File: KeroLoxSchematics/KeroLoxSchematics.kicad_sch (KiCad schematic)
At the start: 49 parts, among them J1 Ignitor1_Output, J2 Ignitor2_Output, M1 LOX_Injector, M2 LOX_Dump, M3 LOX_Vent_Valve, M4 Kero_Vent_Valve, U10 Kero_Tank_PT, U11 LOX_Inj_Line_PT, U12 Kero_Inj_Line_PT, U13 Combusion_Chamber_PT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

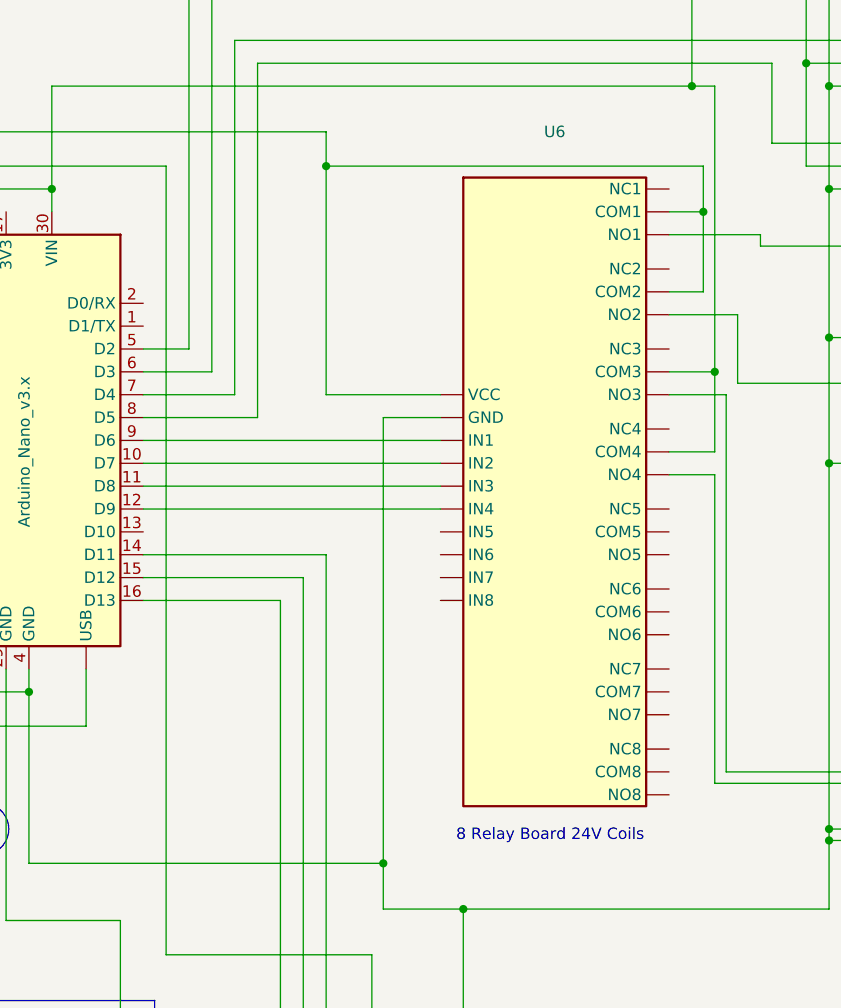
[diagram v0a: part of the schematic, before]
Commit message: Small Change in Relay Board Wiring
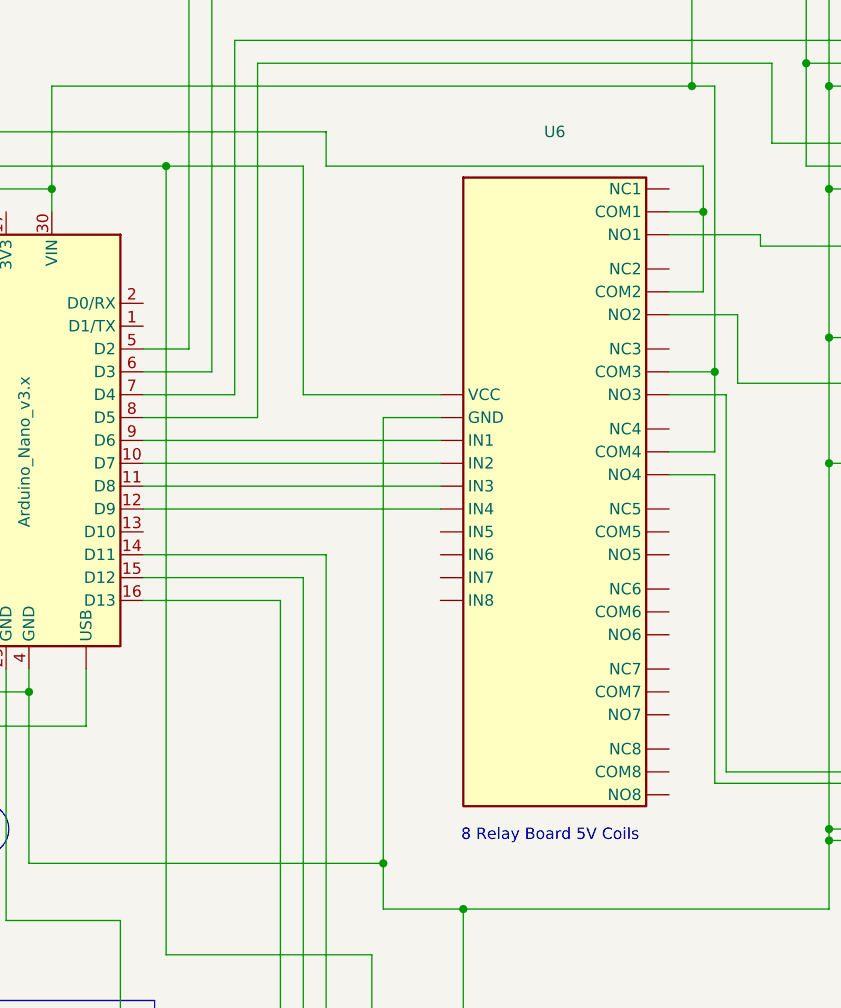
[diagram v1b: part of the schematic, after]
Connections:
- net at U15.9 (SHIELD): no longer U17.9 (SHIELD)
- net at U14.9 (SHIELD): now also U16.9 (SHIELD)
- net at A1.27 (+5V), U18.3 (CS), U18.6 (5V): now also U6. (NO8)
- new net: U15.9 (SHIELD), U17.9 (SHIELD)
- new net: U19. (Ethernet4), U20. (POE_OUT)
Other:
- note added: "8 Relay Board 5V Coils"
- note removed: "8 Relay Board 24V Coils"
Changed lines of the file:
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@@
 		)
 	)
-	(text "8 Relay Board 24V Coils"
+	(text "8 Relay Board 5V Coils"
 		(exclude_from_sim no)
 		(at 441.452 211.582 0)
@@
 	)
 	(junction
-		(at 416.56 137.16)
-		(diameter 0)
-		(color 255 153 0 1)
-	)
-	(junction
 		(at 393.7 238.76)
 		(diameter 0)
@@
 	)
 	(junction
+		(at 398.78 137.16)
+		(diameter 0)
+		(color 72 72 0 1)
+	)
+	(junction
 		(at 316.23 162.56)
 		(diameter 0)
@@
 	(wire
 		(pts
+			(xy 414.02 137.16) (xy 414.02 162.56)
+		)
+		(stroke
+			(width 0)
+			(type default)
+			(color 128 77 0 1)
+		)
+	)
+	(wire
+		(pts
 			(xy 147.32 207.01) (xy 173.99 207.01)
 		)
@@
 	(wire
 		(pts
-			(xy 416.56 137.16) (xy 416.56 162.56)
-		)
-		(stroke
-			(width 0)
-			(type default)
-			(color 255 153 0 1)
-		)
-	)
-	(wire
-		(pts
 			(xy 349.25 140.97) (xy 346.71 140.97)
 		)
@@
 	(wire
 		(pts
-			(xy 416.56 162.56) (xy 429.26 162.56)
-		)
-		(stroke
-			(width 0)
-			(type default)
-			(color 255 153 0 1)
-		)
-	)
-	(wire
-		(pts
 			(xy 214.63 181.61) (xy 226.06 181.61)
 		)
@@
 	(wire
 		(pts
+			(xy 414.02 162.56) (xy 429.26 162.56)
+		)
+		(stroke
+			(width 0)
+			(type default)
+			(color 128 77 0 1)
+		)
+	)
+	(wire
+		(pts
 			(xy 222.25 139.7) (xy 222.25 111.76)
 		)
@@
 		)
 	)
+	(wire
+		(pts
+			(xy 398.78 137.16) (xy 414.02 137.16)
+		)
+		(stroke
+			(width 0)
+			(type default)
+			(color 128 77 0 1)
+		)
+	)

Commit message: Rev'd schematics
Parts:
- added SW1, SW2: SW_SPST, symbol Switch:SW_SPST
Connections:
- net GSE Box Chassis is gone; now on an unnamed net: U17.9 (SHIELD)
- net GND: no longer U16.9 (SHIELD)
- net GSE_BATTERY_24V: now also SW1.1 (A); no longer R13.1, U19. (Ethernet4), U2.1 (Vin), U20. (POE_OUT), U3.1 (Vin)
- net at U14.9 (SHIELD): now also U16.9 (SHIELD)
- new net: R13.1, SW2.2 (B), U2.1 (Vin), U3.1 (Vin)
- new net: U15.9 (SHIELD), U17.9 (SHIELD)
- new net: U14.9 (SHIELD), U16.9 (SHIELD)
- new net: SW1.2 (B), SW2.1 (A), U19. (Ethernet4), U20. (POE_OUT)
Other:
- moved on the sheet: A1, BT1, BT2, BT3, J1, J2, M1, M2, M3, M4, R1, R10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

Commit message: Add laptop connecton
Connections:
- new net: U15.9 (SHIELD), U17.9 (SHIELD)
- new net: U14.9 (SHIELD), U16.9 (SHIELD)
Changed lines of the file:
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@@
+	(wire
+		(pts
+			(xy 40.64 104.14) (xy 67.31 104.14)
+		)
+		(stroke
+			(width 0)
+			(type default)
+			(color 255 0 255 1)
+		)
+	)
 	(wire
 		(pts
@@
 			(type default)
 			(color 0 0 0 1)
+		)
+	)
+	(wire
+		(pts
+			(xy 67.31 99.06) (xy 67.31 104.14)
+		)
+		(stroke
+			(width 0)
+			(type default)
+			(color 255 0 255 1)
 		)
 	)
@@
 		(effects
 			(font
+				(size 1.27 1.27)
+			)
+			(justify left bottom)
+		)
+	)
+	(label "TO_LAPTOP"
+		(at 29.21 107.95 0)
+		(effects
+			(font

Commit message: mistake fix
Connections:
- net GSE_5V: no longer U1.0 (GPIO26), U1.1 (5V), U14.1 (VCC), U14.16 (VDD), U15.1 (VCC), U15.16 (VDD), U2. (GND)
- new net: U15.9 (SHIELD), U17.9 (SHIELD)
- new net: U1.1 (5V), U14.1 (VCC), U14.16 (VDD), U15.1 (VCC), U15.16 (VDD), U2. (GND)
- new net: U14.9 (SHIELD), U16.9 (SHIELD)
- new net: U1.0 (GPIO26), U2. (GND)
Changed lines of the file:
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@@
 	)
 	(junction
-		(at 176.53 125.73)
-		(diameter 0)
-		(color 255 0 0 1)
-	)
-	(junction
 		(at 349.25 257.81)
 		(diameter 0)
@@
 		(at 176.53 213.36)
 		(diameter 0)
-		(color 0 0 0 0)
+		(color 255 0 0 1)
 	)
 	(junction
@@
 	)
 	(junction
+		(at 176.53 125.73)
+		(diameter 0)
+		(color 255 0 0 1)
+	)
+	(junction
 		(at 173.99 118.11)
 		(diameter 0)
@@
 		(color 0 0 0 1)
 	)
-	(junction
-		(at 176.53 109.22)
-		(diameter 0)
-		(color 255 0 0 1)
-	)
 	(wire
 		(pts
@@
 	(wire
 		(pts
+			(xy 179.07 101.6) (xy 176.53 101.6)
+		)
+		(stroke
+			(width 0)
+			(type default)
+			(color 255 0 0 1)
+		)
+	)
+	(wire
+		(pts
 			(xy 402.59 199.39) (xy 402.59 193.04)
 		)
@@
 	(wire
 		(pts
+			(xy 176.53 121.92) (xy 179.07 121.92)
+		)
+		(stroke
+			(width 0)
+			(type default)
+			(color 255 0 0 1)
+		)
+	)
+	(wire
+		(pts
 			(xy 533.4 203.2) (xy 530.86 203.2)
 		)
@@
 			(width 0)
 			(type default)
-			(color 255 0 0 1)
+			(color 0 0 0 1)
 		)
 	)
@@
 	(wire
 		(pts
-			(xy 176.53 101.6) (xy 176.53 109.22)
-		)
-		(stroke
-			(width 0)
-			(type default)
-			(color 255 0 0 1)
-		)
-	)
-	(wire
-		(pts
 			(xy 450.85 255.27) (xy 424.18 255.27)
 		)
@@
 			(width 0)
 			(type default)
-			(color 255 0 0 1)
+			(color 0 0 0 1)
 		)
 	)
@@
 			(width 0)
 			(type default)
-			(color 255 0 0 1)
+			(color 0 0 0 1)
 		)
 	)
@@
 	(wire
 		(pts
+			(xy 176.53 125.73) (xy 176.53 121.92)
+		)
+		(stroke
+			(width 0)
+			(type default)
+			(color 255 0 0 1)
+		)
+	)
+	(wire
+		(pts
 			(xy 485.14 170.18) (xy 491.49 170.18)
 		)
@@
 	(wire
 		(pts
-			(xy 176.53 109.22) (xy 176.53 125.73)
-		)
-		(stroke
-			(width 0)
-			(type default)
-			(color 255 0 0 1)
-		)
-	)
-	(wire
-		(pts
 			(xy 377.19 238.76) (xy 378.46 238.76)
 		)
@@
 		)
 	)
+	(wire
+		(pts
+			(xy 179.07 121.92) (xy 179.07 101.6)
+		)
+		(stroke
+			(width 0)
+			(type default)
+			(color 255 0 0 1)
+		)
+	)

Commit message: Add steppers
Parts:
- removed M2: LOX_Dump, symbol Motor:Motor_Servo
- removed M4: Kero_Vent_Valve, symbol Motor:Motor_Servo
- added U25, U26: ~, symbol KeroLox_Stepper:DM332T_Driver
- added U27, U28: ~, symbol KeroLox_Stepper:NEMA-17_Stepper
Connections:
- net ROCKET_12.6V: now also U25. (B-), U26. (B-)
- net at A1.4 (GND), J1.2 (Pin_2), J2.2 (Pin_2)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: now also U25. (B-), U26. (B-)
- net at A1.8 (D5): now also U26. (B-)
- net at A1.13 (D10): now also U25. (B-)
- net at A1.14 (D11): now also U26. (B-); no longer U18.8 (DAT1)
- net at A1.26 (A7): now also U18.8 (DAT1)
- net at A1.27 (+5V), U18.3 (CS), U18.6 (5V)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: now also U25. (B-), U26. (B-)
- net at A1.6 (D3): now also U25. (B-)
- new net: U15.9 (SHIELD), U17.9 (SHIELD)
- new net: U14.9 (SHIELD), U16.9 (SHIELD)
- new net: U25. (B-), U27. (B-) (x4)
- new net: U26. (B-), U28. (B-) (x4)

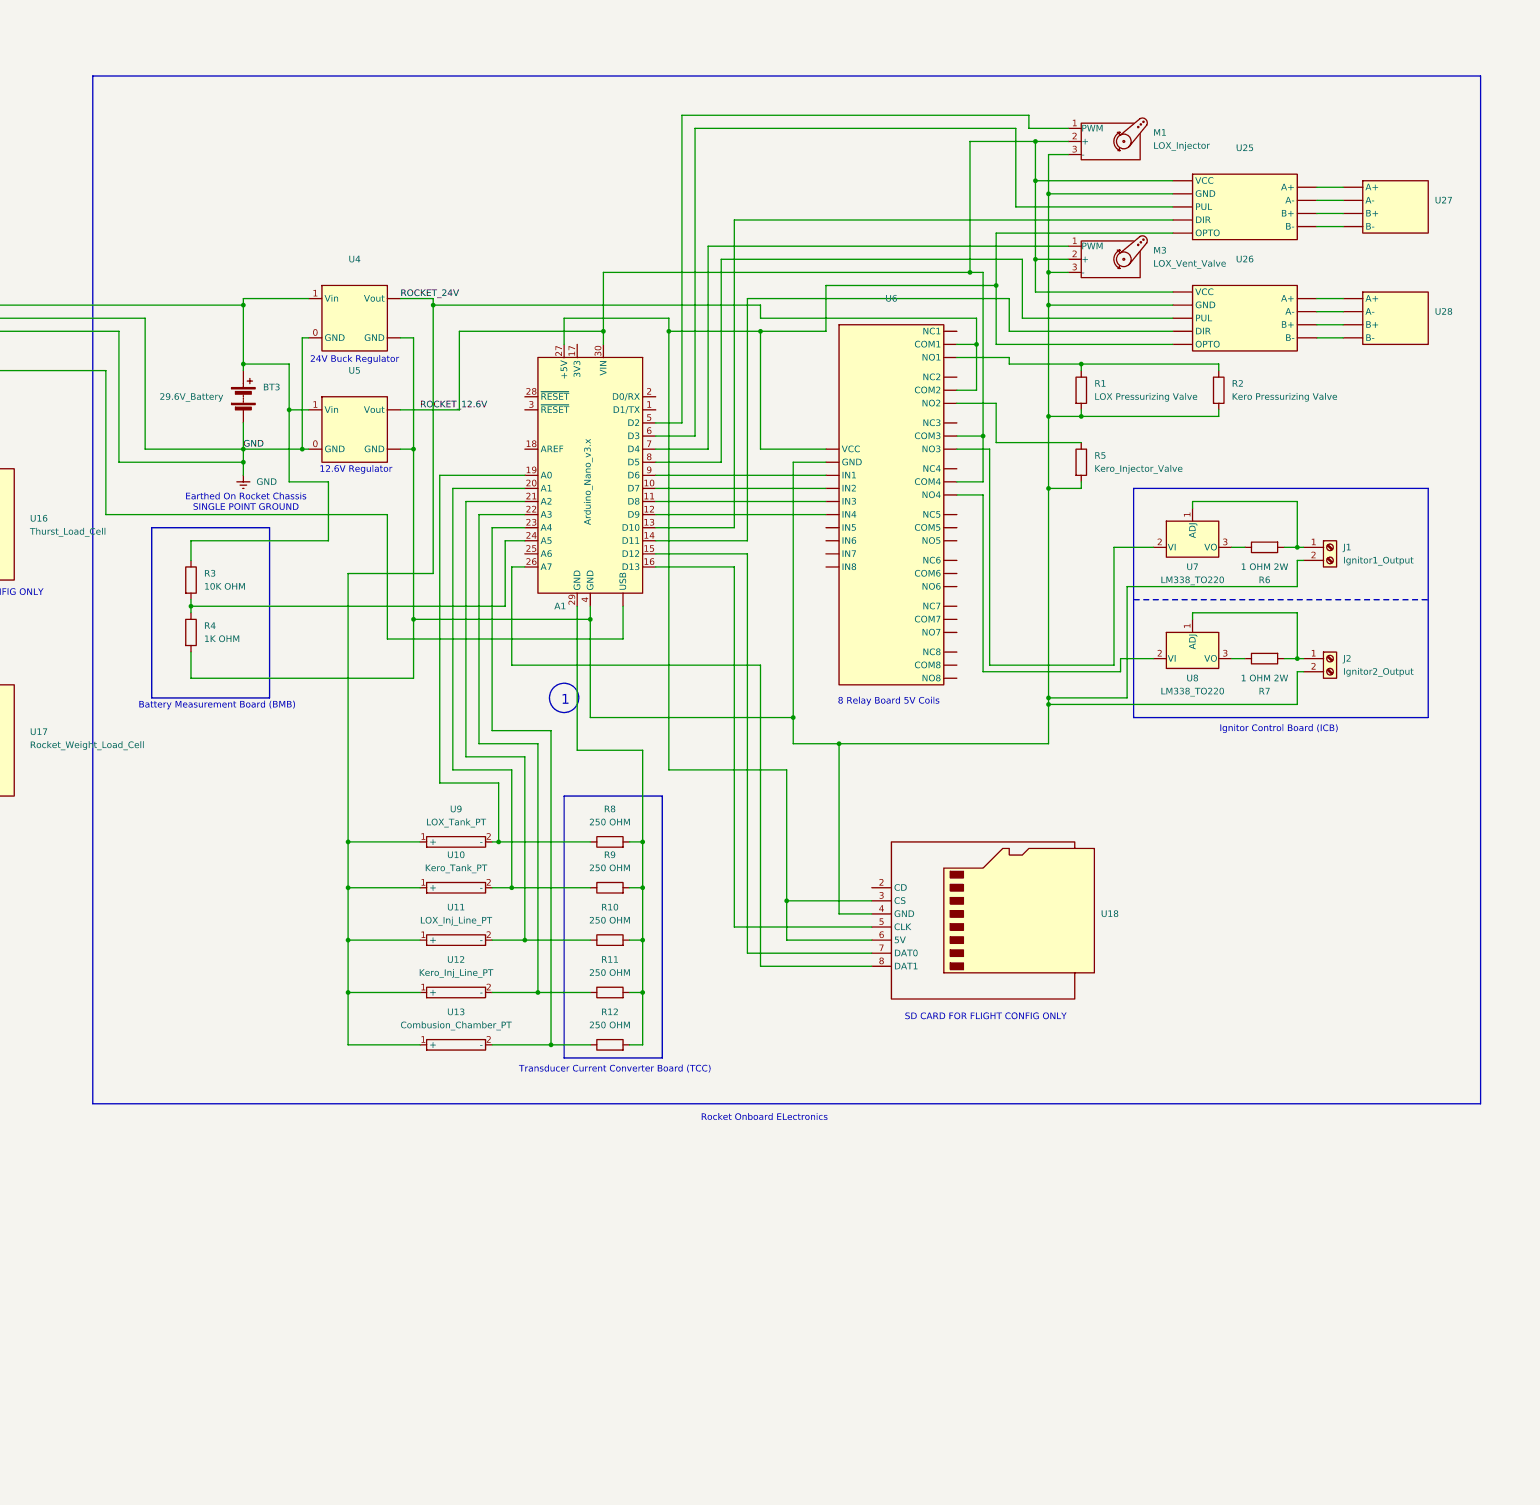
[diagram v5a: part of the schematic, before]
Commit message: Move valves, ignitor, and pts out of rocket electrical section
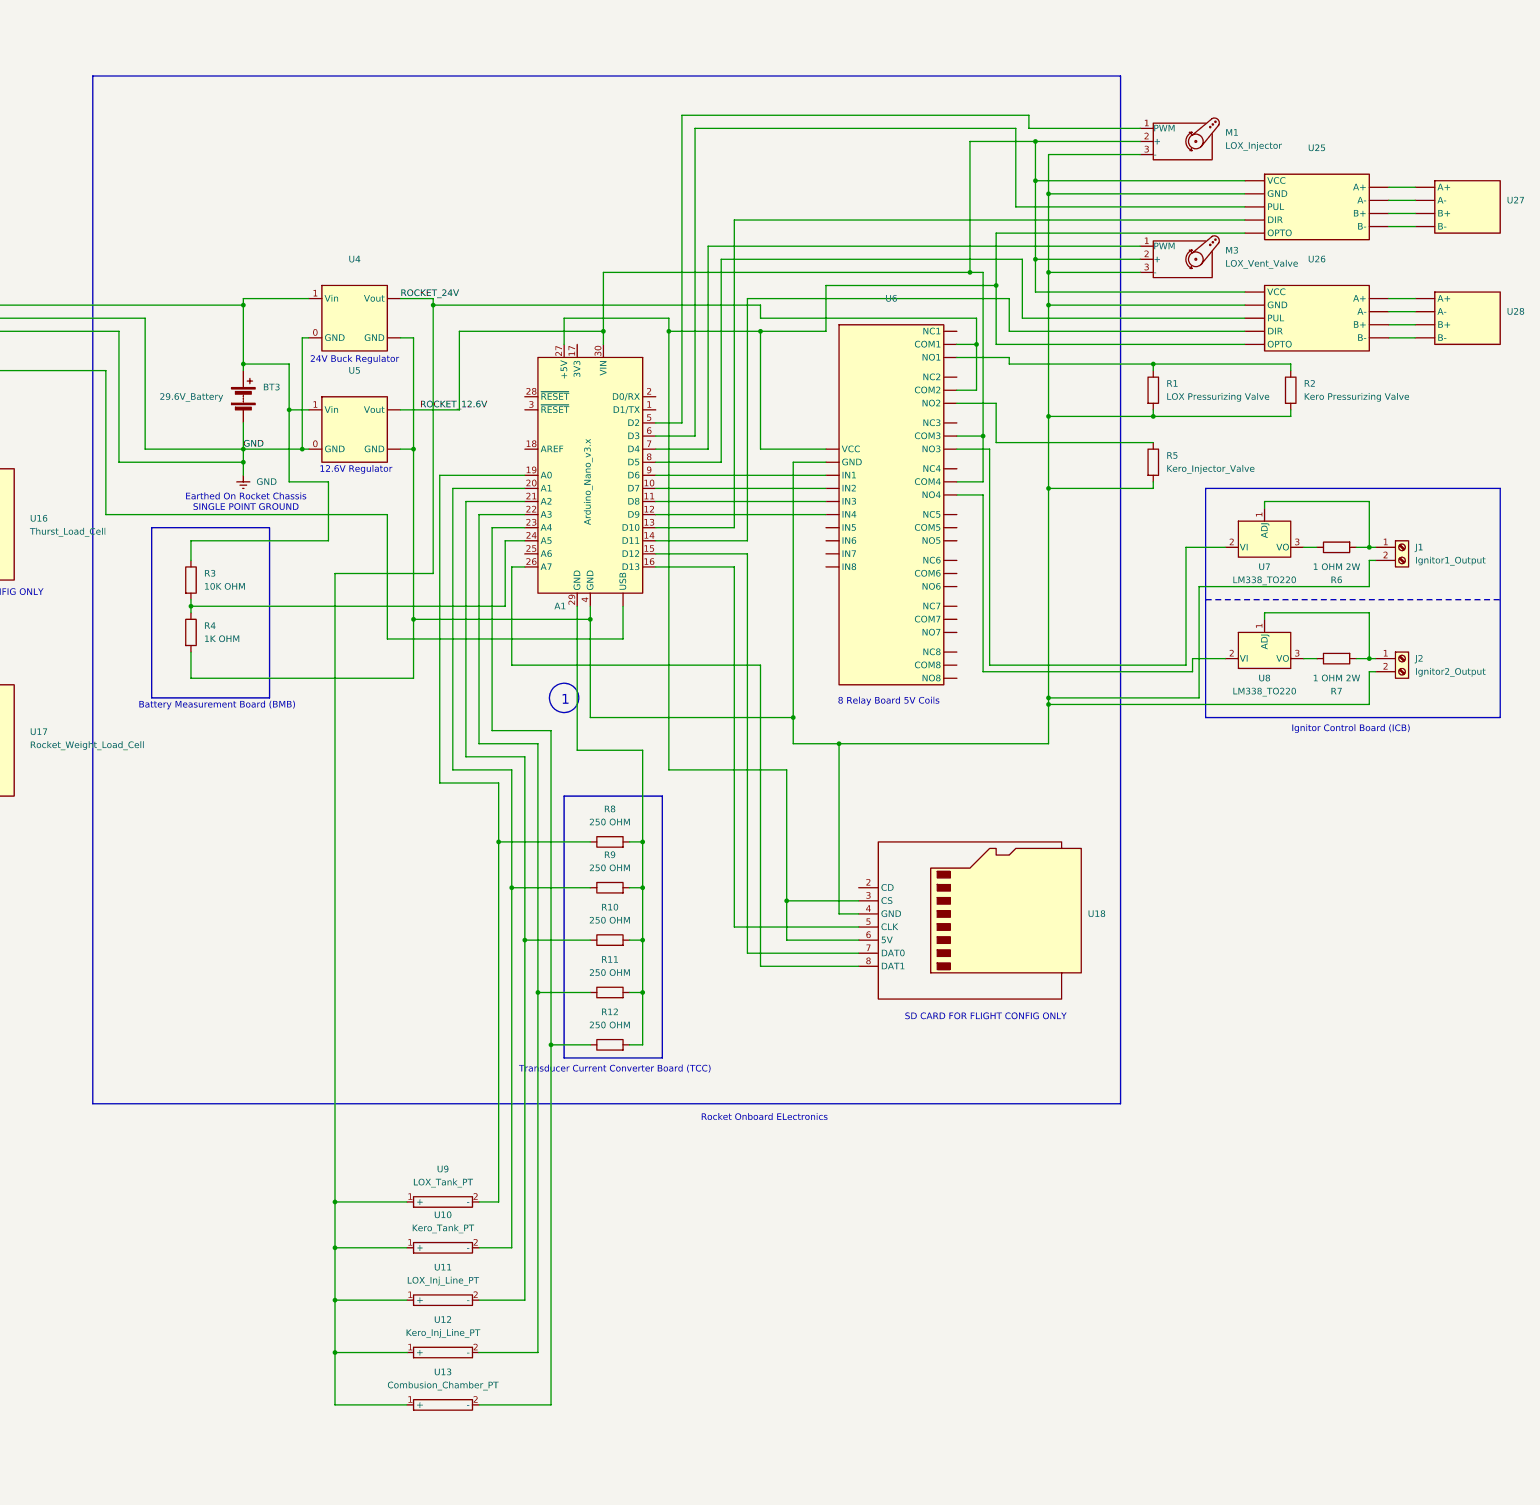
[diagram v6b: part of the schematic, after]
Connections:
- new net: U15.9 (SHIELD), U17.9 (SHIELD)
- new net: U14.9 (SHIELD), U16.9 (SHIELD)
- new net: U25. (B-), U27. (B-) (x3)
- new net: U26. (B-), U28. (B-) (x3)
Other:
- moved on the sheet: J1, J2, M1, M3, R1, R2, R5, R6, R7, U10, U11, U12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

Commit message: Small Fix and names
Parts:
- U25: value ~ -> LOX_Dump_Stepper_Driver
- U26: value ~ -> KERO_Vent_Stepper_Driver
- U27: value ~ -> LOX_Dump_Stepper_Motor
- U28: value ~ -> Kero_Vent_Stepper_Motor
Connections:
- new net: U15.9 (SHIELD), U17.9 (SHIELD)
- new net: U14.9 (SHIELD), U16.9 (SHIELD)
- new net: U25. (B-), U27. (B-) (x3)
- new net: U26. (B-), U28. (B-) (x3)
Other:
- moved on the sheet: A1, BT1, BT2, BT3, BT4, J1, J2, M1, M3, R1, R10, R11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
